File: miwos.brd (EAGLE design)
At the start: 120 x 120 mm, 44 parts

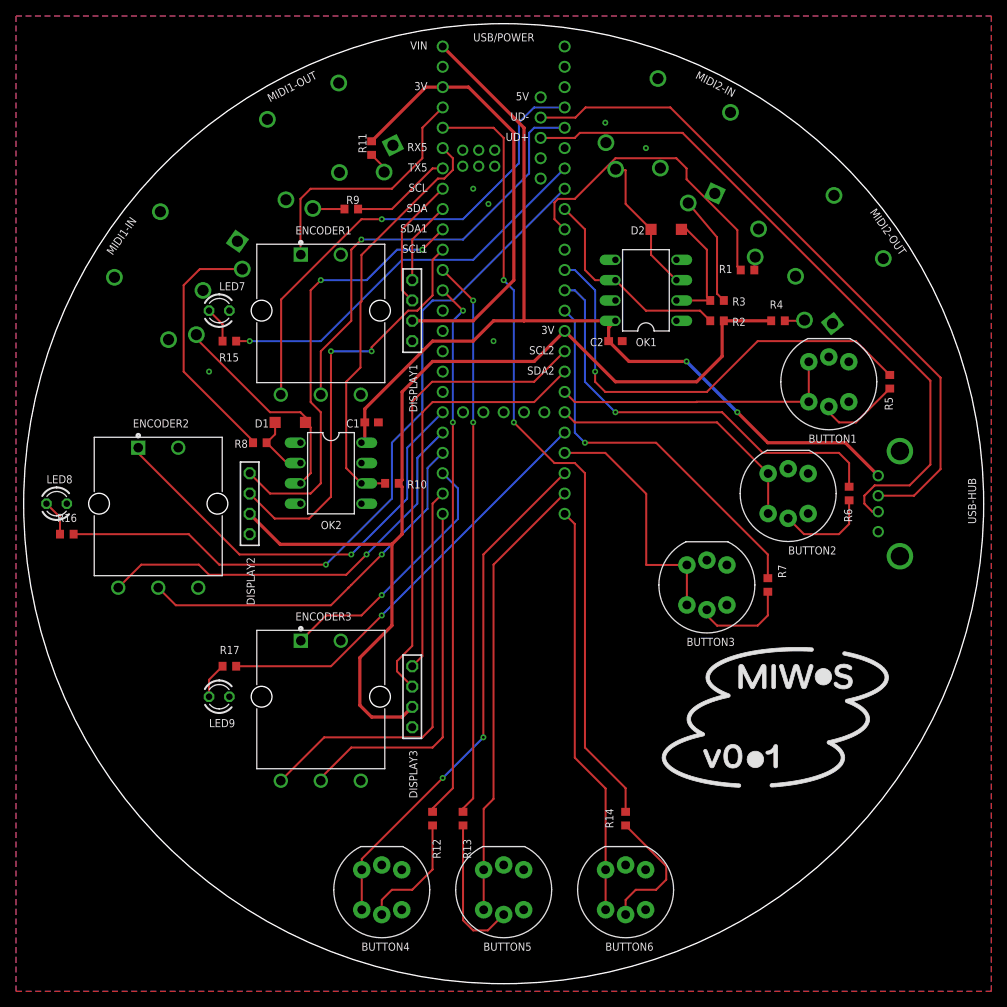
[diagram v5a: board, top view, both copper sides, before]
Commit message: Rearrange midi jacks and encoders/displays
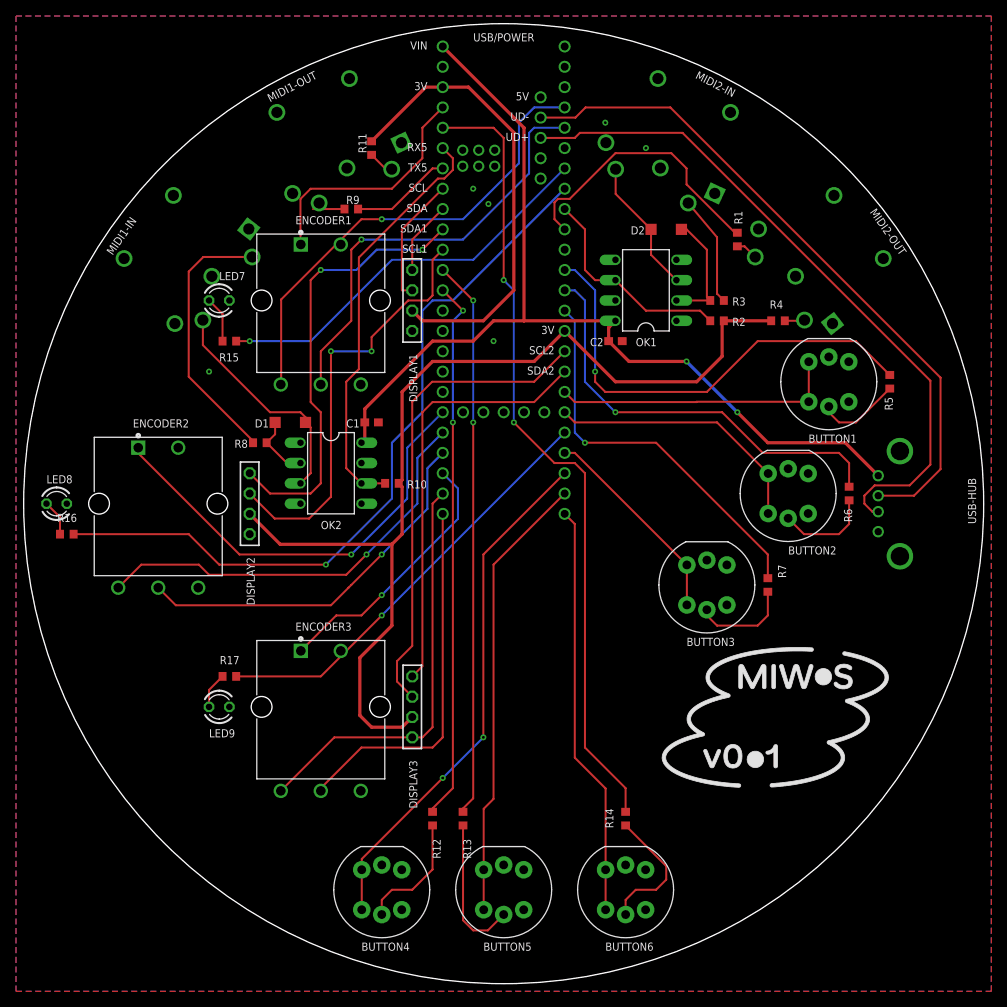
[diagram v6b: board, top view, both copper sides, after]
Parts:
- moved R1 4.02 mm to (29.2, 33.0), turned to 90 degrees
- moved MIDI1-IN 2.35 mm to (-40.4, 31.5), turned to 218 degrees
- moved MIDI1-OUT 1.28 mm to (-21.7, 46.5), turned to 245 degrees
- moved DISPLAY1 1.27 mm to (-11.4, 25.4)
- moved DISPLAY3 1.27 mm to (-11.4, -25.4)
- moved ENCODER1 1.27 mm to (-22.9, 25.4)
- moved ENCODER3 1.27 mm to (-22.9, -25.4)
- moved LED7 1.27 mm to (-35.6, 25.4)
- moved LED9 1.27 mm to (-35.6, -25.4)
- moved R17 1.27 mm to (-34.3, -21.6)
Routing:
- net BUTTON3: track 31.3 -> 26.1 mm
- net TX2: track 38.7 -> 34.6 mm
- net +3V3: track 182.5 -> 185.0 mm
- net N$10: track 31.4 -> 33.4 mm
- net N$9: track 27.3 -> 28.8 mm
- net SCL2: track 58.8 -> 60.1 mm
- net SDA2: track 52.2 -> 53.4 mm
- net ENCODER1-B: track 55.7 -> 54.4 mm
- net SDA: track 10.5 -> 9.20 mm
- net N$4: track 4.51 -> 5.78 mm
- net ENCODER1-PUSH: track 31.7 -> 30.5 mm
- net ENCODER1-A: track 60.3 -> 59.0 mm
- net N$19: track 1.65 -> 2.78 mm
- net N$11: track 3.99 -> 4.93 mm
- net SDA1: track 54.8 -> 55.5 mm
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
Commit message: Use DFR0647 displays
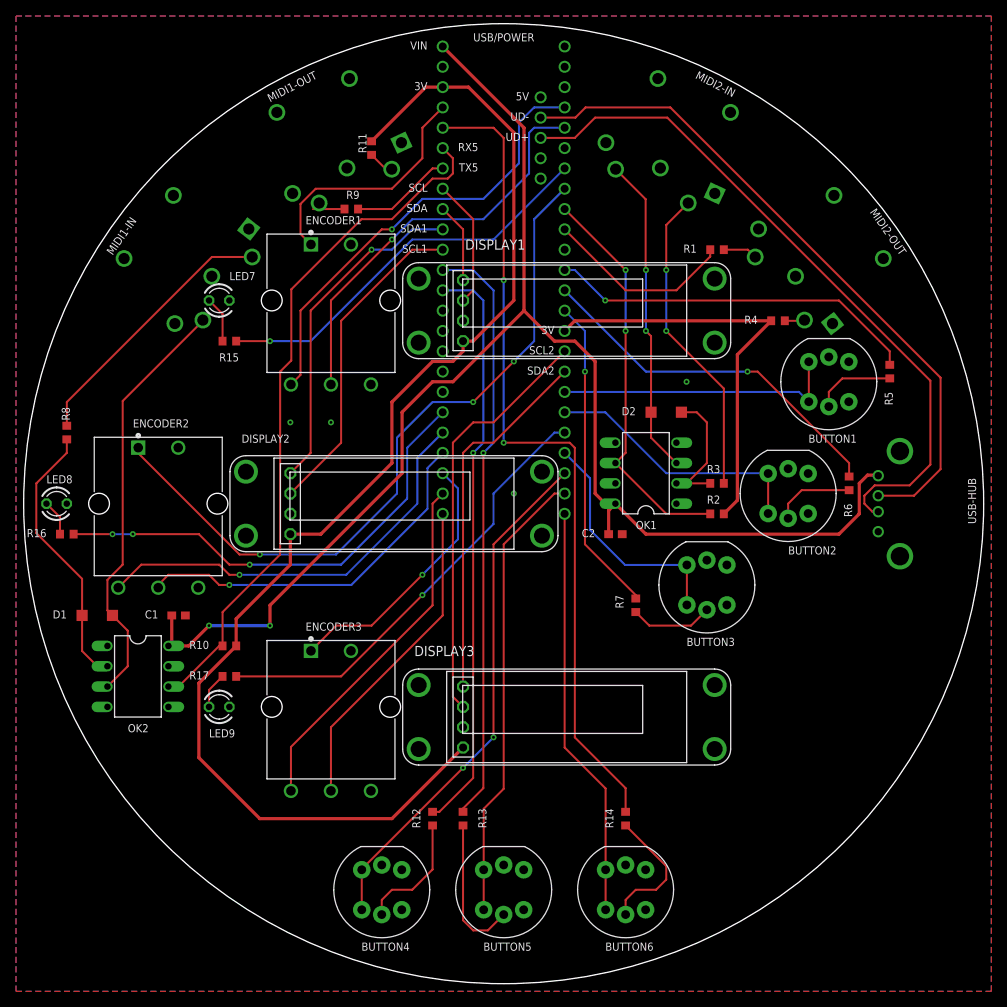
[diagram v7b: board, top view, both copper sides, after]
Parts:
- DISPLAY1, DISPLAY2, DISPLAY3: value OLED-DISPLAY -> DFR0647; device oled-display:OLED-DISPLAY -> DFR0647:DFR0647
- moved OK2 35.0 mm to (-45.7, -21.6)
- moved C1 34.1 mm to (-40.6, -14.0)
- moved D1 34.1 mm to (-50.8, -14.0)
- moved R10 28.7 mm to (-34.3, -17.8)
- moved R8 24.2 mm to (-54.6, 8.89), turned to 270 degrees
- moved C2 24.1 mm to (14.0, -3.81)
- moved R2 24.1 mm to (26.7, -1.27)
- moved OK1 22.9 mm to (17.8, 3.81)
- moved D2 22.9 mm to (20.3, 11.4)
- moved R3 22.9 mm to (26.7, 2.54)
- moved DISPLAY3 19.3 mm to (7.87, -26.7), turned to 0 degrees
- moved DISPLAY1 19.3 mm to (7.87, 24.1), turned to 0 degrees
- moved DISPLAY2 18.0 mm to (-13.7, 0.00), turned to 0 degrees
- moved R7 16.7 mm to (16.5, -12.7)
- moved R1 2.84 mm to (26.7, 31.8), turned to 180 degrees
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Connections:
- net +3V3: now also DISPLAY1.VCC, DISPLAY2.VCC, DISPLAY3.VCC; no longer DISPLAY1.3, DISPLAY2.3, DISPLAY3.3
- net ENCODER2-LED: now also TEENSY-41.38; no longer TEENSY-41.6
- net ENCODER2-PUSH: now also TEENSY-41.6; no longer TEENSY-41.38
- net GND: now also DISPLAY1.GND, DISPLAY2.GND, DISPLAY3.GND; no longer DISPLAY1.4, DISPLAY2.4, DISPLAY3.4
- net SCL: now also DISPLAY1.SCL; no longer DISPLAY1.2
- net SCL1: now also DISPLAY2.SCL; no longer DISPLAY2.2
- net SCL2: now also DISPLAY3.SCL; no longer DISPLAY3.2
- net SDA: now also DISPLAY1.SDA; no longer DISPLAY1.1
- net SDA1: now also DISPLAY2.SDA; no longer DISPLAY2.1
- net SDA2: now also DISPLAY3.SDA; no longer DISPLAY3.1
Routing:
- net +5V: track 122.4 -> 184.0 mm
- net ENCODER2-PUSH: track 55.1 -> 91.2 mm, vias 1 -> 3
- net RX5: track 52.2 -> 86.9 mm
- net ENCODER2-LED: track 94.0 -> 59.3 mm, vias 1 -> 3
- net +3V3: track 185.0 -> 214.6 mm
- net N$8: track 8.26 -> 34.4 mm
- net N$18: track 13.8 -> 39.2 mm, vias 0 -> 2
- net N$9: track 28.8 -> 52.9 mm
- net RX2: track 27.0 -> 49.9 mm, vias 0 -> 2
- net N$17: track 17.0 -> 39.9 mm, vias 0 -> 2
- net SDA1: track 55.5 -> 42.1 mm, vias 2 -> 1
- net SCL1: track 53.6 -> 40.6 mm, vias 2 -> 0
- net BUTTON1-LED: track 58.0 -> 46.5 mm
- net TX2: track 34.6 -> 24.0 mm
- net BUTTON3-LED: track 49.2 -> 39.7 mm
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
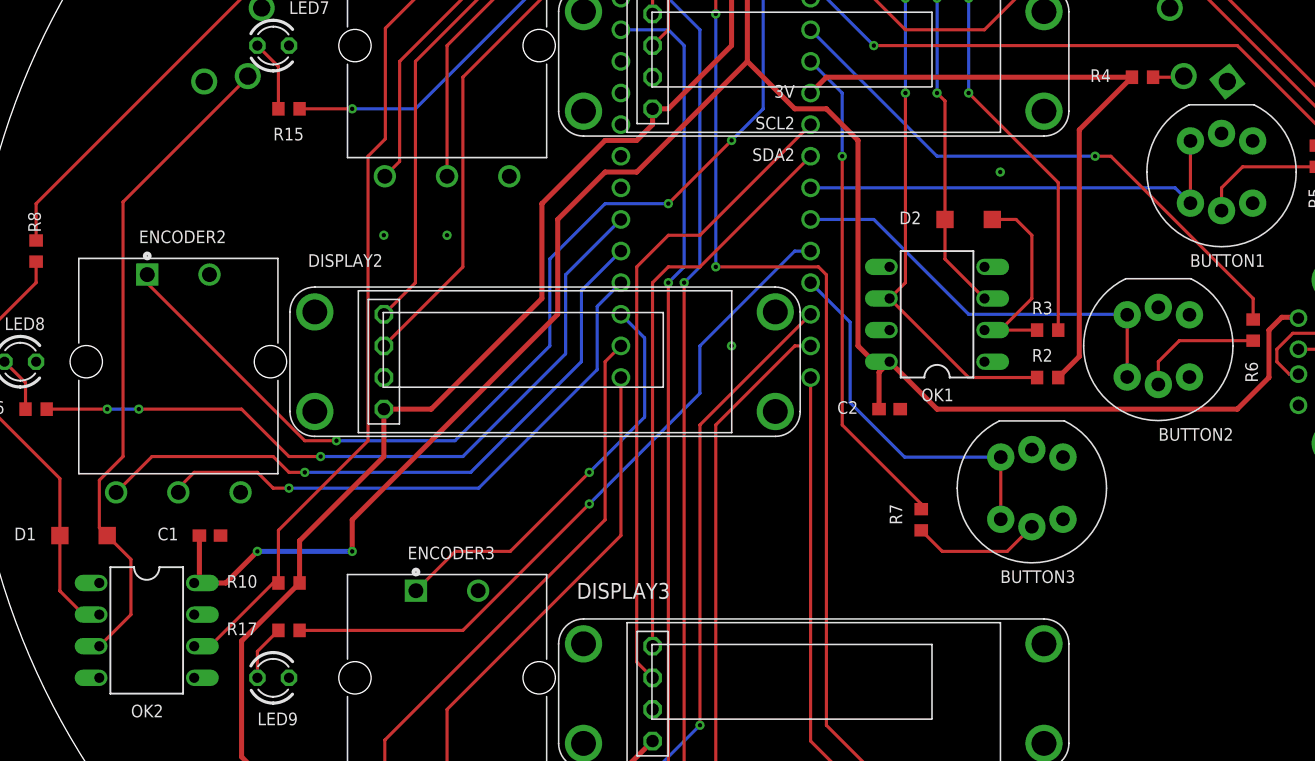
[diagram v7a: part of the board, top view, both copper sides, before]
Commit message: Use 6N138 SMD footprint
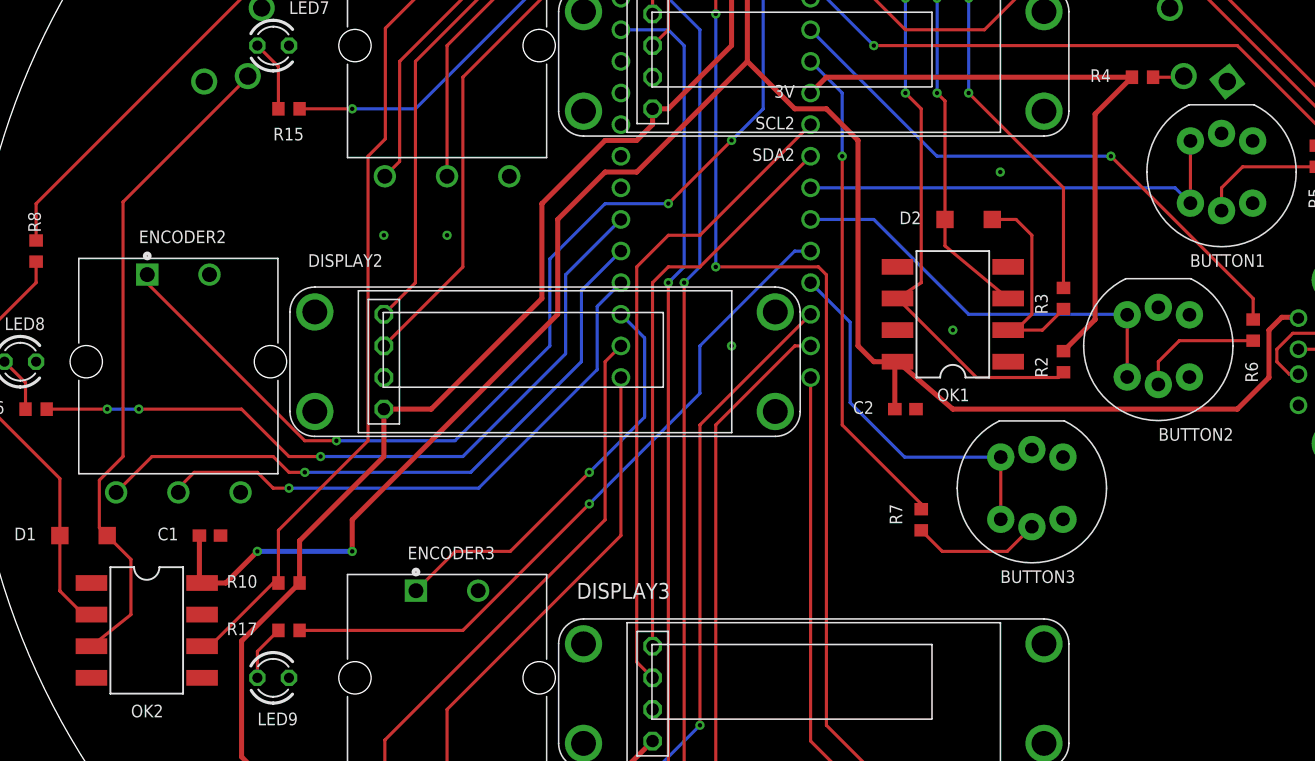
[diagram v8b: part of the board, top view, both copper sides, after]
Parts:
- OK1, OK2: device optocoupler:DIL08 -> 6N138:DIL08
- moved R3 2.84 mm to (27.9, 5.08), turned to 270 degrees
- moved R2 1.80 mm to (27.9, 0.00), turned to 270 degrees
- moved C2 1.27 mm to (15.2, -3.81)
- moved OK1 1.27 mm to (19.1, 3.81)
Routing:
- net N$18: track 39.2 -> 35.9 mm
- net RX2: track 49.9 -> 52.6 mm
- net +3V3: track 214.6 -> 212.3 mm
- net +5V: track 184.0 -> 182.8 mm
- net N$17: track 39.9 -> 40.9 mm
- net N$8: track 34.4 -> 33.7 mm
- net RX5: track 86.9 -> 86.3 mm
